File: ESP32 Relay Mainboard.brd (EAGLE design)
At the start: 129 x 100 mm, 91 parts, among them J2 AUDIO_JACK_TRRSSMD_RA, J3 AUDIO_JACK_TRRSSMD_RA, J4 AUDIO_JACK_TRRSSMD_RA, J5 AUDIO_JACK_TRRSSMD_RA, J6 AUDIO_JACK_TRRSSMD_RA, K1 SRD-05VDC-SL-C, K2 SRD-05VDC-SL-C, K3 SRD-05VDC-SL-C, K4 SRD-05VDC-SL-C, K5 SRD-05VDC-SL-C, K6 SRD-05VDC-SL-C, U1 ESP32-S2-WROOM, U2 CP2104, U4 LM2576SX-5.0/NOPB

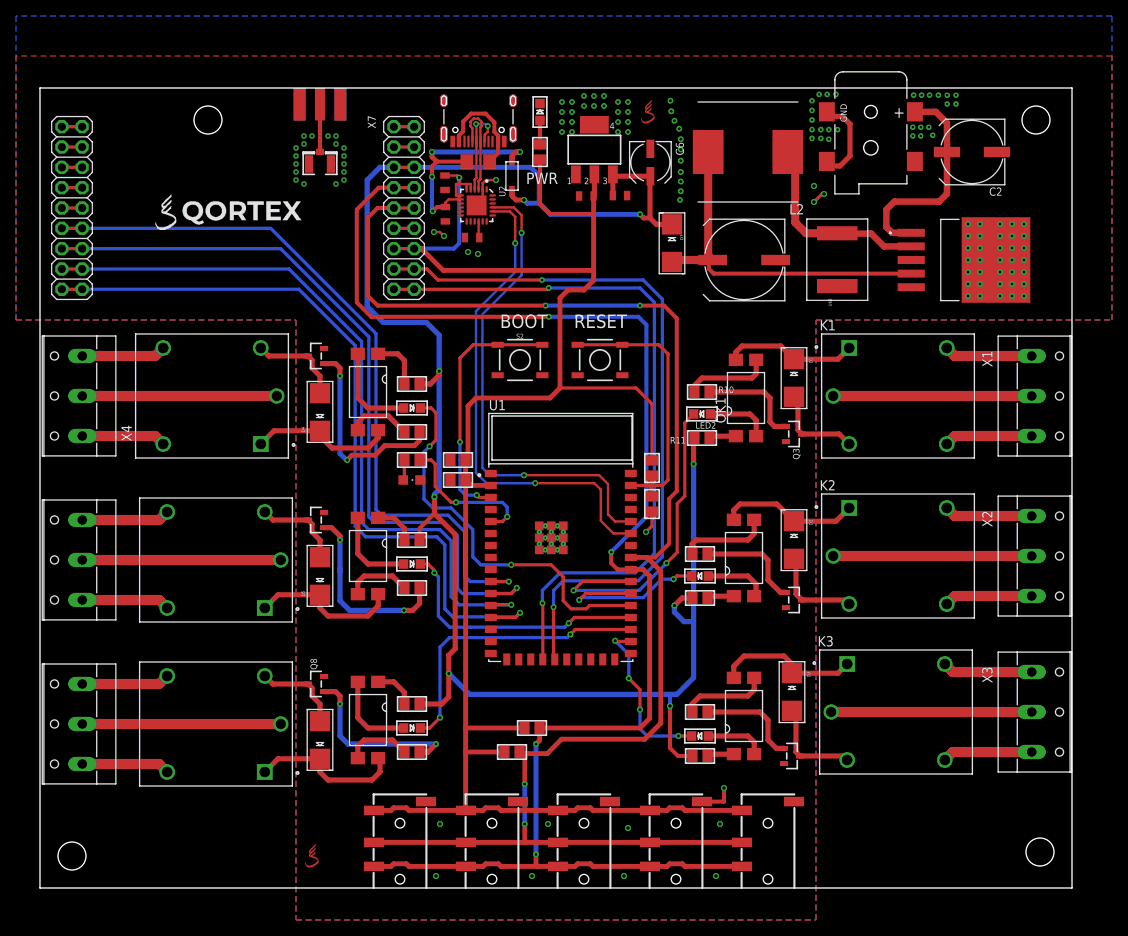
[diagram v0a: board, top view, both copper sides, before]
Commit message: Add files via upload
Added second UART port. Added OTG usb. Removed CP2102. Added 6th jack connector. Added labels.
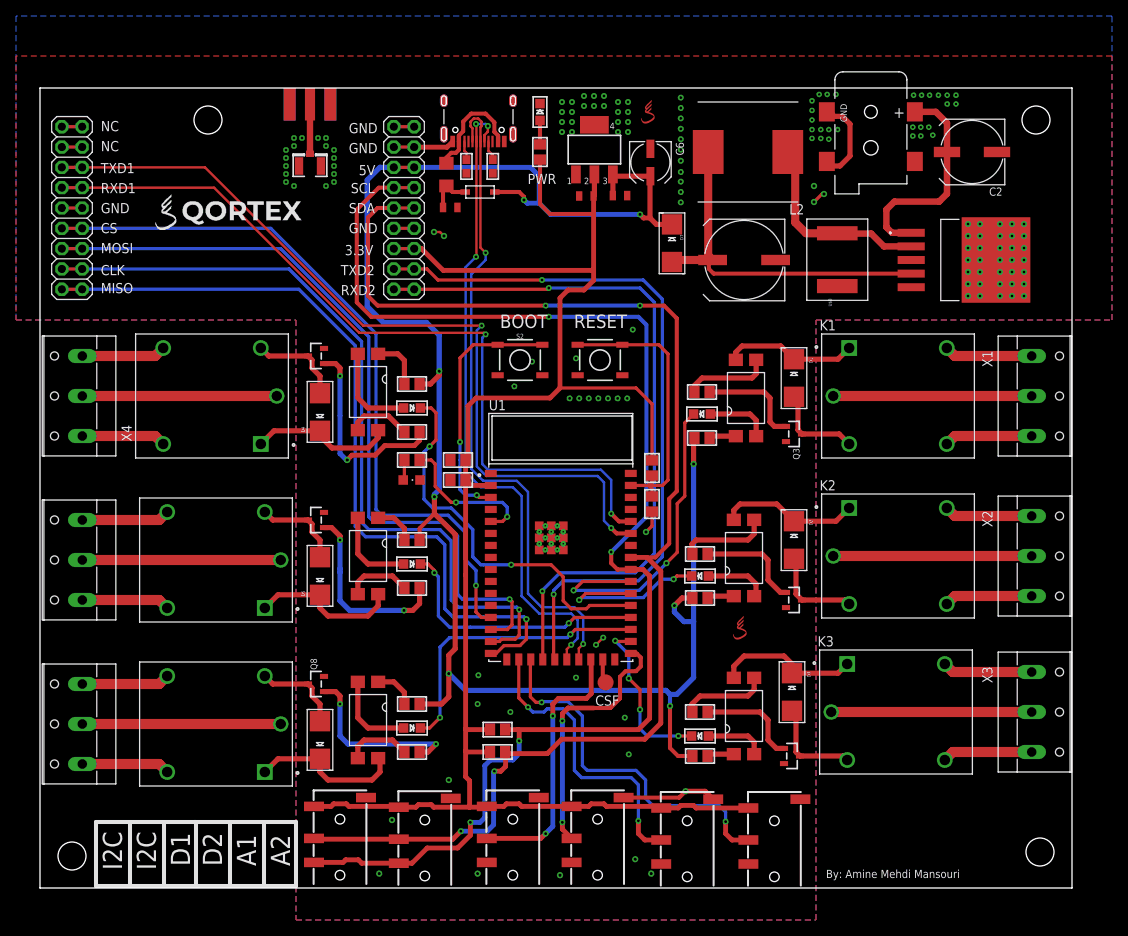
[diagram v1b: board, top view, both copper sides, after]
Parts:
- removed C4: 4.7uF, SparkFun-Capacitors:0805
- removed C5: 0.1uF, SparkFun-Capacitors:0805
- removed U2: CP2104, microbuilder:QFN24_4MM_SMSC
- added J1: AUDIO_JACK_TRRSSMD_RA, SparkFun-Connectors:AUDIO_JACK_3.5MM_TRRS_SMD_RA
- added R3, R6: 5.1K, microbuilder:0603
- added TP1: TPTP20R, testpad:TP20R
- moved U$27 60.6 mm to (118.5, 32.5)
- moved J2 10.1 mm to (111.9, -0.20)
- moved J6 9.81 mm to (100.7, 0.00)
- moved J5 8.91 mm to (90.1, 0.00)
- moved J3 8.41 mm to (79.1, -0.10)
- moved J4 7.52 mm to (68.5, 0.00)
- moved D8 4.47 mm to (86.0, 87.0), turned to 180 degrees
- moved R1 4.30 mm to (88.2, 19.8)
- moved F2 4.30 mm to (81.8, 89.2), turned to 270 degrees
- moved R2 1.80 mm to (88.2, 17.0)
- moved X8 1.27 mm to (64.8, 90.2)
- moved X7 1.25 mm to (64.8, 100.0)
- moved C1 1.05 mm to (82.3, 85.1), turned to 0 degrees
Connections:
- removed net DTR: U2.23
- removed net GPIO13: U1.16
- removed net N$167: JP4.10, JP4.9
- removed net N$168: JP4.11, JP4.12
- removed net N$170: JP4.13, JP4.14
- removed net RTS: U2.19
- removed net RXD: U1.37, U2.20
- removed net TXD: U1.38, U2.21
- new net ADC1: J2.RING1, U1.18
- new net ADC2: J1.RING1, U1.19
- new net GPIO21: J5.RING1, U1.24
- new net GPIO33: J6.RING1, U1.27
- new net N$10: CONN1.A5, R6.2
- new net N$17: TP1.TP, U1.25
- new net NC1: J5.RING2
- new net NC2: J6.RING2
- new net NC3: J1.RING2
- new net NC4: J2.RING2
- new net RXD1: JP4.13, JP4.14, U1.37
- new net TXD1: JP4.11, JP4.12, U1.38
- net +3V3: now also J1.TIP; no longer C5.1, U2.5, U2.6, U2.7
- net CLK: now also U1.15; no longer U1.12
- net CS: now also U1.13; no longer U1.10
- net D+: now also U1.23; no longer U2.3
- net D-: now also U1.22; no longer U2.4
- net GND: now also J1.EARTH, JP4.10, JP4.9, R3.1, R6.1; no longer C4.2, C5.2, U2.2, U2.THERM
- net MISO: now also U1.16; no longer U1.13
- net MOSI: now also U1.14; no longer U1.11
- net N$13: now also CONN1.B5, R3.2; no longer C4.1, U2.16
- net SCL: no longer J2.RING2, J5.RING2, J6.RING2
- net SDA: no longer J2.RING1, J5.RING1, J6.RING1
- net VBUS: no longer U2.8
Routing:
- net RXD1: track 0.00 -> 105.0 mm, vias 0 -> 2
- net TXD1: track 0.00 -> 100.9 mm, vias 0 -> 2
- net D+: track 12.9 -> 83.4 mm, vias 0 -> 2
- net D-: track 12.0 -> 82.3 mm, vias 2 -> 4
- net RXD: track 61.9 -> 0.00 mm, vias 2 -> 0
- net TXD: track 61.2 -> 0.00 mm, vias 2 -> 0
- net ADC2: track 0.00 -> 46.1 mm, vias 0 -> 2
- net ADC1: track 0.00 -> 37.6 mm, vias 0 -> 2
- net GPIO21: track 0.00 -> 33.8 mm, vias 0 -> 2
- net GPIO33: track 0.00 -> 32.5 mm, vias 0 -> 2
- net VBUS: track 29.0 -> 5.53 mm, vias 4 -> 0
- net SDA: track 188.2 -> 165.9 mm
- net SCL: track 191.0 -> 170.2 mm
- net +3V3: track 235.8 -> 216.3 mm, vias 1 -> 0
- net GND: track 34.5 -> 46.0 mm, vias 18 -> 73
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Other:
- board text added: "3.3V"
- board text added: "5V"
- board text added: "A1"
- board text added: "A2"
- board text added: "By: Amine Mehdi Mansouri"
- board text added: "CLK"
- board text added: "CS"
- board text added: "CSF"
- board text added: "D1"
- board text added: "D2"
- board text added: "GND"
- board text added: "I2C"
- board text added: "MISO"
- board text added: "MOSI"
- board text added: "NC"
- board text added: "RXD1"
- board text added: "RXD2"
- board text added: "SCL"
- board text added: "SDA"
- board text added: "TXD1"
- board text added: "TXD2"

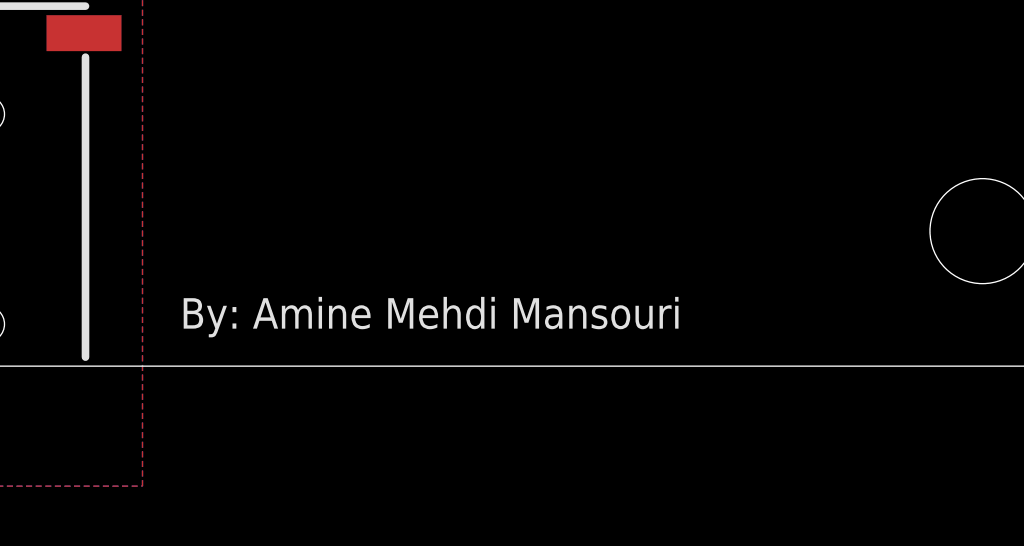
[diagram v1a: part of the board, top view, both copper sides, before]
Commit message: Updated the schematic with values
Added values to components (resistors and caps). Also added a description to some parts of the board.
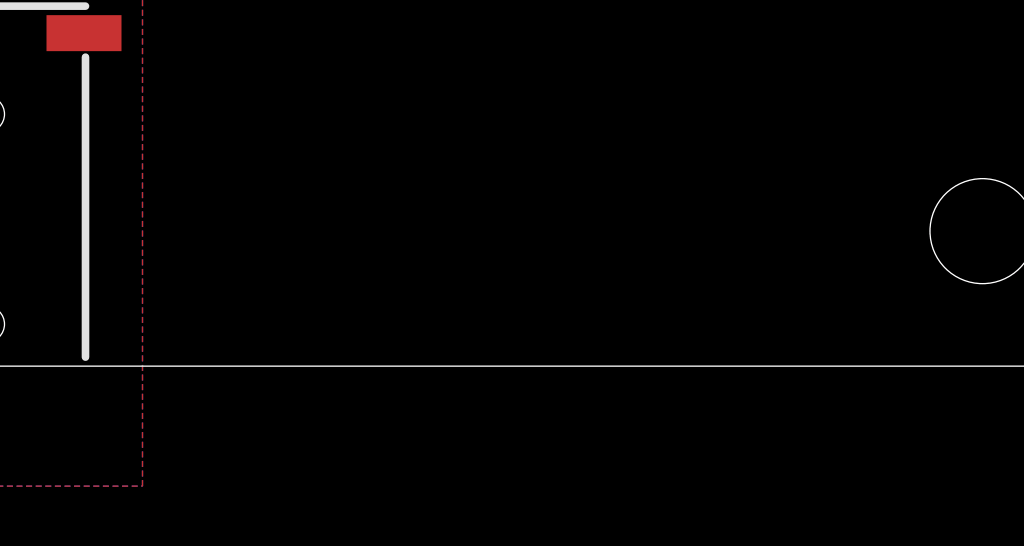
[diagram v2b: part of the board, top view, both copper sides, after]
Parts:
- C10, C9: value (none) -> 0.1uF
- C11: value (none) -> 0.1uf
- C2, C6: value (none) -> 10uF
- C3: value (none) -> 100uF
- R10, R11, R12, R13, R15, R16, R17, R18, R19, R20, R21: value (none) -> 1k
- R14, R22, R5: value (none) -> 1K
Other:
- board text removed: "By: Amine Mehdi Mansouri"
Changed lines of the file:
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@@
 <drawing>
 <settings>
-<setting alwaysvectorfont="yes"/>
+<setting alwaysvectorfont="no"/>
 <setting verticaltext="up"/>
 </settings>
@@
 <text x="58" y="2.75" size="2.4" layer="25" font="vector" ratio="15" rot="R90">A1</text>
 <text x="62.25" y="2.75" size="2.4" layer="25" font="vector" ratio="15" rot="R90">A2</text>
-<text x="129.25" y="1.25" size="1.016" layer="25" font="vector" ratio="15">By: Amine Mehdi Mansouri</text>
 </plain>
 <attributes>
@@
 <attribute name="VALUE" x="76.18" y="48.46" size="1.27" layer="27"/>
 </element>
-<element name="R5" library="microbuilder" package="0805" value="" x="77.5" y="53.5" smashed="yes" rot="R180">
+<element name="R5" library="microbuilder" package="0805" value="1K" x="77.5" y="53.5" smashed="yes" rot="R180">
 <attribute name="VALUE" x="75.468" y="54.262" size="0.4064" layer="27" ratio="10" rot="R180"/>
 </element>
@@
 <attribute name="SF_ID" value="PRT-12639" x="100.7" y="0" size="1.778" layer="27" rot="R90" display="off"/>
 </element>
-<element name="C9" library="microbuilder" package="0805" value="" x="107.5" y="48" smashed="yes" rot="R270">
+<element name="C9" library="microbuilder" package="0805" value="0.1uF" x="107.5" y="48" smashed="yes" rot="R270">
 <attribute name="VALUE" x="106.738" y="45.968" size="0.4064" layer="27" ratio="10" rot="R270"/>
 </element>
-<element name="C10" library="microbuilder" package="0805" value="" x="83.25" y="53.5" smashed="yes">
+<element name="C10" library="microbuilder" package="0805" value="0.1uF" x="83.25" y="53.5" smashed="yes">
 <attribute name="VALUE" x="85.282" y="52.738" size="0.4064" layer="27" ratio="10"/>
 </element>
-<element name="C11" library="microbuilder" package="0805" value="" x="83.25" y="51" smashed="yes">
+<element name="C11" library="microbuilder" package="0805" value="0.1uf" x="83.25" y="51" smashed="yes">
 <attribute name="VALUE" x="85.282" y="50.238" size="0.4064" layer="27" ratio="10"/>
 </element>
@@
 <attribute name="POPULARITY" value="0" x="119.25" y="61.25" size="1.778" layer="27" display="off"/>
 </element>
-<element name="R10" library="microbuilder" package="0805" value="" x="113.75" y="62" smashed="yes">
+<element name="R10" library="microbuilder" package="0805" value="1k" x="113.75" y="62" smashed="yes">
 <attribute name="VALUE" x="115.782" y="61.238" size="0.4064" layer="27" ratio="10"/>
 </element>
@@
 <attribute name="VALUE" x="124.615" y="54.972" size="0.4064" layer="27" ratio="10" rot="R270"/>
 </element>
-<element name="R11" library="microbuilder" package="0805" value="" x="113.75" y="56.25" smashed="yes" rot="R180">
+<element name="R11" library="microbuilder" package="0805" value="1k" x="113.75" y="56.25" smashed="yes" rot="R180">
 <attribute name="VALUE" x="111.718" y="57.012" size="0.4064" layer="27" ratio="10" rot="R180"/>
 </element>
@@
 <attribute name="POPULARITY" value="0" x="109.5" y="73.75" size="1.778" layer="27" display="off"/>
 </element>
-<element name="R12" library="microbuilder" package="0805" value="" x="113.5" y="41.75" smashed="yes">
+<element name="R12" library="microbuilder" package="0805" value="1k" x="113.5" y="41.75" smashed="yes">
 <attribute name="VALUE" x="115.532" y="40.988" size="0.4064" layer="27" ratio="10"/>
 </element>
@@
 <attribute name="VALUE" x="124.615" y="34.222" size="0.4064" layer="27" ratio="10" rot="R270"/>
 </element>
-<element name="R13" library="microbuilder" package="0805" value="" x="113.5" y="36.25" smashed="yes" rot="R180">
+<element name="R13" library="microbuilder" package="0805" value="1k" x="113.5" y="36.25" smashed="yes" rot="R180">
 <attribute name="VALUE" x="111.468" y="37.012" size="0.4064" layer="27" ratio="10" rot="R180"/>
 </element>
@@
 <attribute name="POPULARITY" value="0" x="109.5" y="54" size="1.778" layer="27" display="off"/>
 </element>
-<element name="R14" library="microbuilder" package="0805" value="" x="113.5" y="22" smashed="yes">
+<element name="R14" library="microbuilder" package="0805" value="1K" x="113.5" y="22" smashed="yes">
 <attribute name="VALUE" x="115.532" y="21.238" size="0.4064" layer="27" ratio="10"/>
 </element>
@@
 <attribute name="VALUE" x="124.365" y="14.722" size="0.4064" layer="27" ratio="10" rot="R270"/>
 </element>
-<element name="R15" library="microbuilder" package="0805" value="" x="113.5" y="16.5" smashed="yes" rot="R180">
+<element name="R15" library="microbuilder" package="0805" value="1k" x="113.5" y="16.5" smashed="yes" rot="R180">
 <attribute name="VALUE" x="111.468" y="17.262" size="0.4064" layer="27" ratio="10" rot="R180"/>
 </element>
@@
 <attribute name="POPULARITY" value="0" x="81.5" y="29.5" size="1.778" layer="27" rot="R180" display="off"/>
 </element>
-<element name="R16" library="microbuilder" package="0805" value="" x="77.5" y="57" smashed="yes">
+<element name="R16" library="microbuilder" package="0805" value="1k" x="77.5" y="57" smashed="yes">
 <attribute name="VALUE" x="79.532" y="56.238" size="0.4064" layer="27" ratio="10"/>
 </element>
@@
 <attribute name="VALUE" x="66.135" y="68.278" size="0.4064" layer="27" ratio="10" rot="R90"/>
 </element>
-<element name="R17" library="microbuilder" package="0805" value="" x="77.5" y="63" smashed="yes">
+<element name="R17" library="microbuilder" package="0805" value="1k" x="77.5" y="63" smashed="yes">
 <attribute name="VALUE" x="79.532" y="62.238" size="0.4064" layer="27" ratio="10"/>
 </element>
@@
 <attribute name="POPULARITY" value="0" x="81.5" y="9" size="1.778" layer="27" rot="R180" display="off"/>
 </element>
-<element name="R18" library="microbuilder" package="0805" value="" x="77.5" y="37.5" smashed="yes">
+<element name="R18" library="microbuilder" package="0805" value="1k" x="77.5" y="37.5" smashed="yes">
 <attribute name="VALUE" x="79.532" y="36.738" size="0.4064" layer="27" ratio="10"/>
 </element>
@@
 <attribute name="VALUE" x="66.135" y="47.778" size="0.4064" layer="27" ratio="10" rot="R90"/>
 </element>
-<element name="R19" library="microbuilder" package="0805" value="" x="77.5" y="43.5" smashed="yes">
+<element name="R19" library="microbuilder" package="0805" value="1k" x="77.5" y="43.5" smashed="yes">
 <attribute name="VALUE" x="79.532" y="42.738" size="0.4064" layer="27" ratio="10"/>
 </element>
@@
 <attribute name="POPULARITY" value="0" x="81.5" y="-11.5" size="1.778" layer="27" rot="R180" display="off"/>
 </element>
-<element name="R20" library="microbuilder" package="0805" value="" x="77.5" y="17" smashed="yes">
+<element name="R20" library="microbuilder" package="0805" value="1k" x="77.5" y="17" smashed="yes">
 <attribute name="VALUE" x="79.532" y="16.238" size="0.4064" layer="27" ratio="10"/>
 </element>
@@
 <attribute name="VALUE" x="66.135" y="27.278" size="0.4064" layer="27" ratio="10" rot="R90"/>
 </element>
-<element name="R21" library="microbuilder" package="0805" value="" x="77.5" y="23" smashed="yes">
+<element name="R21" library="microbuilder" package="0805" value="1k" x="77.5" y="23" smashed="yes">
 <attribute name="VALUE" x="79.532" y="22.238" size="0.4064" layer="27" ratio="10"/>
 </element>
@@
 <attribute name="VALUE" x="94.897" y="95.222" size="0.4064" layer="27" ratio="10" rot="R90"/>
 </element>
-<element name="R22" library="microbuilder" package="0805" value="" x="93.5" y="92" smashed="yes" rot="R270">
+<element name="R22" library="microbuilder" package="0805" value="1K" x="93.5" y="92" smashed="yes" rot="R270">
 <attribute name="VALUE" x="92.738" y="89.968" size="0.4064" layer="27" ratio="10" rot="R270"/>
 </element>
@@
 <attribute name="PRICE" value="None" x="150.5" y="78.5" size="1.778" layer="27" display="off"/>
 </element>
-<element name="C3" library="rcl" library_urn="urn:adsk.eagle:library:334" package="UD-10X10_NICHICON" package3d_urn="urn:adsk.eagle:package:23469/1" value="" x="119" y="78.5" smashed="yes" rot="R180">
+<element name="C3" library="rcl" library_urn="urn:adsk.eagle:library:334" package="UD-10X10_NICHICON" package3d_urn="urn:adsk.eagle:package:23469/1" value="100uF" x="119" y="78.5" smashed="yes" rot="R180">
 <attribute name="POPULARITY" value="0" x="119" y="78.5" size="1.778" layer="27" rot="R180" display="off"/>
 <attribute name="SPICEPREFIX" value="C" x="119" y="78.5" size="1.778" layer="27" rot="R180" display="off"/>
 <attribute name="VALUE" x="124.08" y="84.85" size="1.016" layer="27" rot="R180"/>
 </element>
-<element name="C2" library="rcl" library_urn="urn:adsk.eagle:library:334" package="UD-8X10_NICHICON" package3d_urn="urn:adsk.eagle:package:23473/1" value="" x="147.5" y="92" smashed="yes" rot="R180">
+<element name="C2" library="rcl" library_urn="urn:adsk.eagle:library:334" package="UD-8X10_NICHICON" package3d_urn="urn:adsk.eagle:package:23473/1" value="10uF" x="147.5" y="92" smashed="yes" rot="R180">
 <attribute name="NAME" x="151.31" y="87.555" size="1.016" layer="25" rot="R180"/>
 <attribute name="POPULARITY" value="0" x="147.5" y="92" size="1.778" layer="27" rot="R180" display="off"/>
@@
 <attribute name="VALUE" x="97.76" y="90.9792" size="1.27" layer="27"/>
 </element>
-<element name="C6" library="rcl" library_urn="urn:adsk.eagle:library:334" package="UD-5X5,8_NICHICON" package3d_urn="urn:adsk.eagle:package:23470/1" value="" x="107.3" y="90.7" smashed="yes" rot="R270">
+<element name="C6" library="rcl" library_urn="urn:adsk.eagle:library:334" package="UD-5X5,8_NICHICON" package3d_urn="urn:adsk.eagle:package:23470/1" value="10uF" x="107.3" y="90.7" smashed="yes" rot="R270">
 <attribute name="NAME" x="110.475" y="93.24" size="1.016" layer="25" rot="R270"/>
 <attribute name="POPULARITY" value="0" x="107.3" y="90.7" size="1.778" layer="27" rot="R270" display="off"/>
